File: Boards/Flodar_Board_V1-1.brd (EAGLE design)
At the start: 66 x 46 mm, 6 parts, among them U1 FEATHER_M0_BASIC_PROTO, U2 LP2981-33DBVR

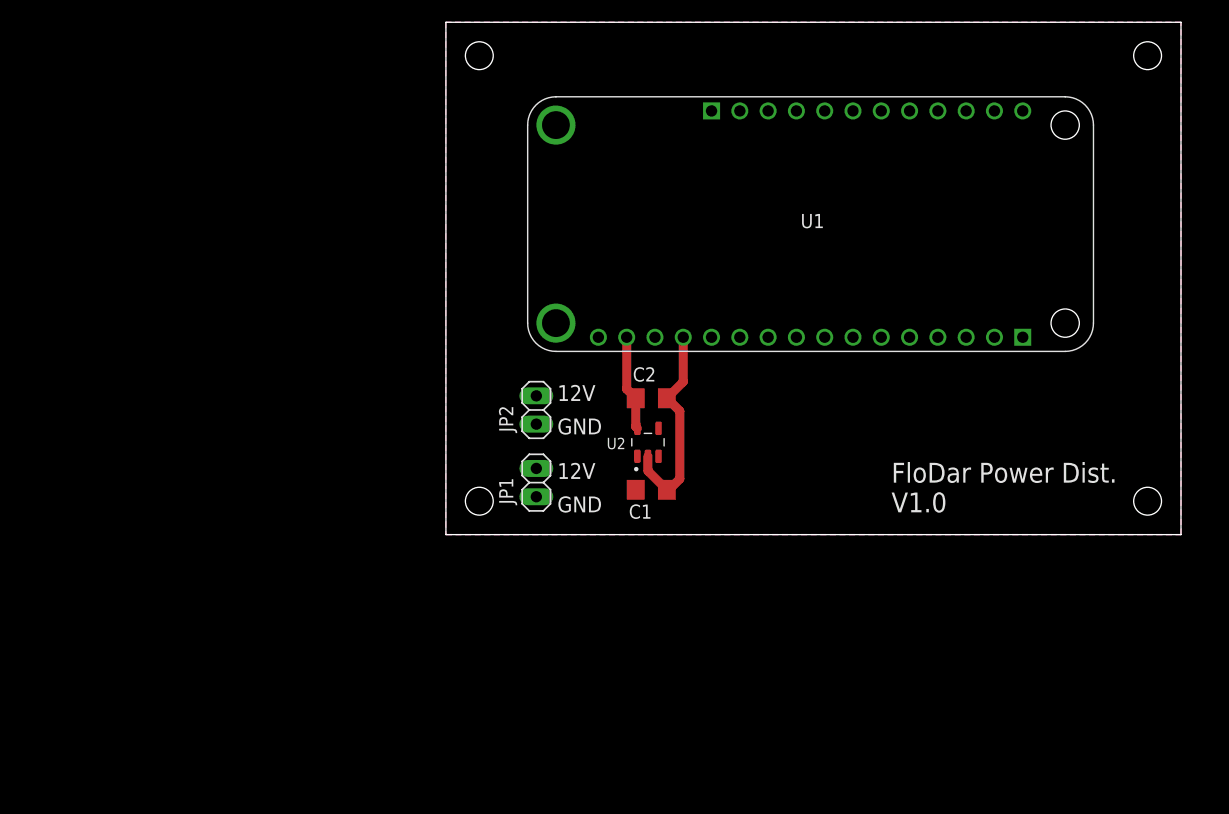
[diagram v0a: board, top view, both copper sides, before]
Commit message: Combine Breakout and Power Dist. Boards
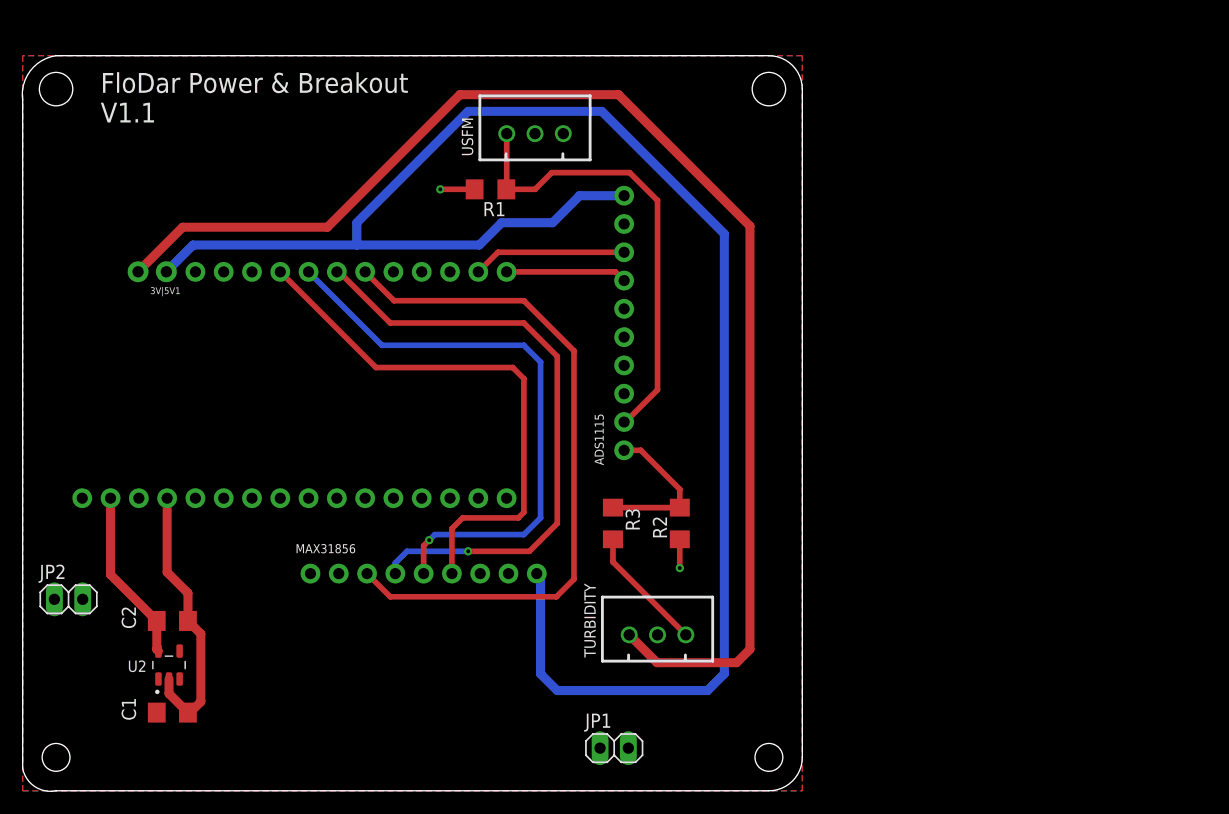
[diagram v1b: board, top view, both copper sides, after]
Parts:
- removed U1: FEATHER_M0_BASIC_PROTO, FEATHER_M0_BASIC_PROTO:MODULE_FEATHER_M0_BASIC_PROTO
- added 3V|5V1: (no value), SparkFun-Connectors:1X02_NO_SILK
- added ADS1115: (no value), microbuilder:1X10_ROUND70
- added MAX31856: (no value), microbuilder:1X09_ROUND_70
- added MS3: FEATHERWING, adafruit_wing:FEATHERWING
- added R1: 150, adafruit:R1206
- added R2: 2.2k, adafruit:R1206
- added R3: 3.3k, adafruit:R1206
- added TURBIDITY, USFM: JST-XH-03-PIN-ROUND-PAD, Rembrandt Electronics - JST XH Connectors v1-0:JST-XH-03-PACKAGE-ROUND-PAD
- moved C1 47.4 mm to (15.4, 13.0)
- moved C2 47.4 mm to (15.4, 21.2)
- moved U2 47.4 mm to (15.1, 17.3)
- moved JP2 45.3 mm to (6.12, 23.2), turned to 0 degrees
- moved JP1 24.8 mm to (55.1, 9.83), turned to 0 degrees
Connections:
- removed net VBAT: U1.P2_1
- removed net VBUS: U1.P2_3
- new net !CS: MAX31856.3, MS3.22
- new net !FAULT: MAX31856.2
- new net AIN2: ADS1115.2, R1.1, USFM.1
- new net AIN3: ADS1115.1, R2.2, R3.1
- new net ALERT: ADS1115.5
- new net DRDY: MAX31856.1
- new net H_3V: 3V|5V1.1, ADS1115.10, MAX31856.9
- new net H_5V: 3V|5V1.2, TURBIDITY.1
- new net SCK: MAX31856.6, MS3.25
- new net SCL: ADS1115.8, MS3.18
- new net SD0: MAX31856.5, MS3.24
- new net SDA: ADS1115.7, MS3.17
- new net SDI: MAX31856.4, MS3.23
- new net SIGNAL: R3.2, TURBIDITY.3
- net 3.3V: now also MS3.2; no longer U1.P1_15
- net GND: now also ADS1115.3, ADS1115.4, ADS1115.6, ADS1115.9, MAX31856.7, MS3.4, R1.2, R2.1, TURBIDITY.2, USFM.2; no longer U1.P1_1, U1.P1_13
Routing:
- net H_3V: track 0.00 -> 154.0 mm
- net H_5V: track 0.00 -> 116.8 mm
- net !CS: track 0.00 -> 62.3 mm
- net SDI: track 0.00 -> 54.9 mm, vias 0 -> 1
- net SD0: track 0.00 -> 52.2 mm, vias 0 -> 1
- net SCK: track 0.00 -> 48.9 mm
- net AIN2: track 0.00 -> 41.4 mm
- net AIN3: track 0.00 -> 14.1 mm
- net SCL: track 0.00 -> 13.8 mm
- net GND: track 19.1 -> 30.5 mm, vias 0 -> 2
- net SIGNAL: track 0.00 -> 11.3 mm
- net SDA: track 0.00 -> 10.9 mm
- net 3.3V: track 8.57 -> 15.5 mm
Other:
- board size 66 x 46 mm -> 70 x 66 mm
- board text added: "FloDar Power & Breakout V1.1"
- board text removed: "12V"
- board text removed: "FloDar Power Dist. V1.0"
- board text removed: "GND"
